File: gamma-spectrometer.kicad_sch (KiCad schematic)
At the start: 36 parts, among them T1 T1-1T-KK81, U1 Pico 2, U2 MAX1422ECM+D, U3 TLV3201AIDBVR, U4 MAX5026EUT_T

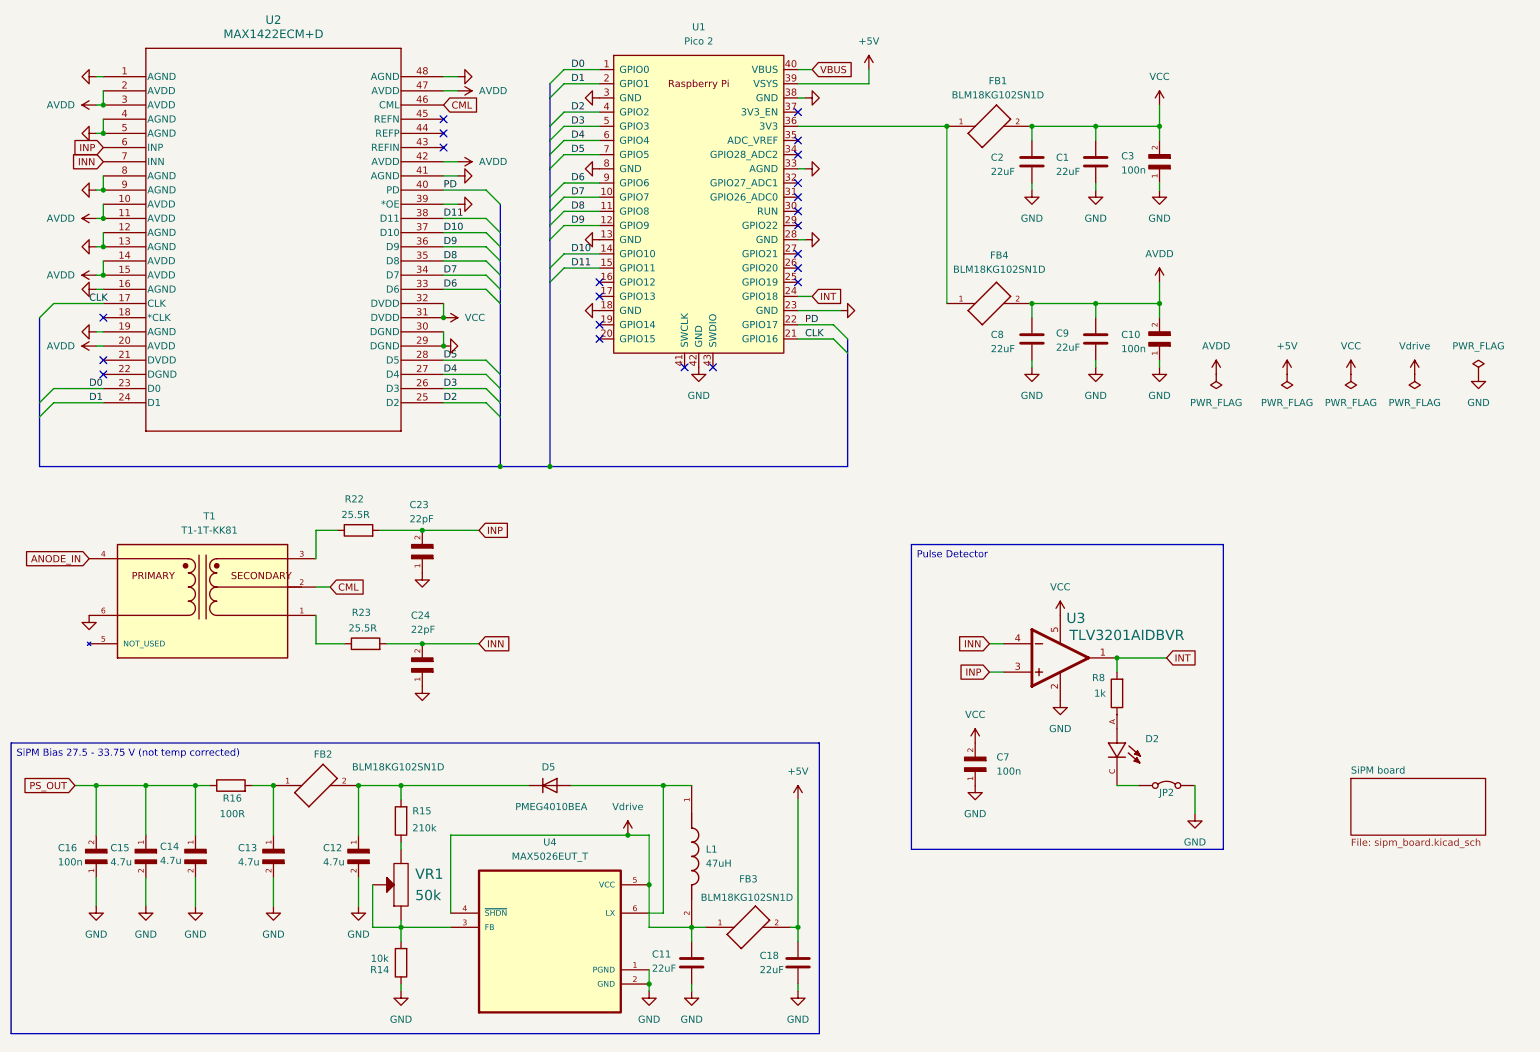
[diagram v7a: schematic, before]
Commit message: MCP41050 replaces pot for SiPM PS regulation
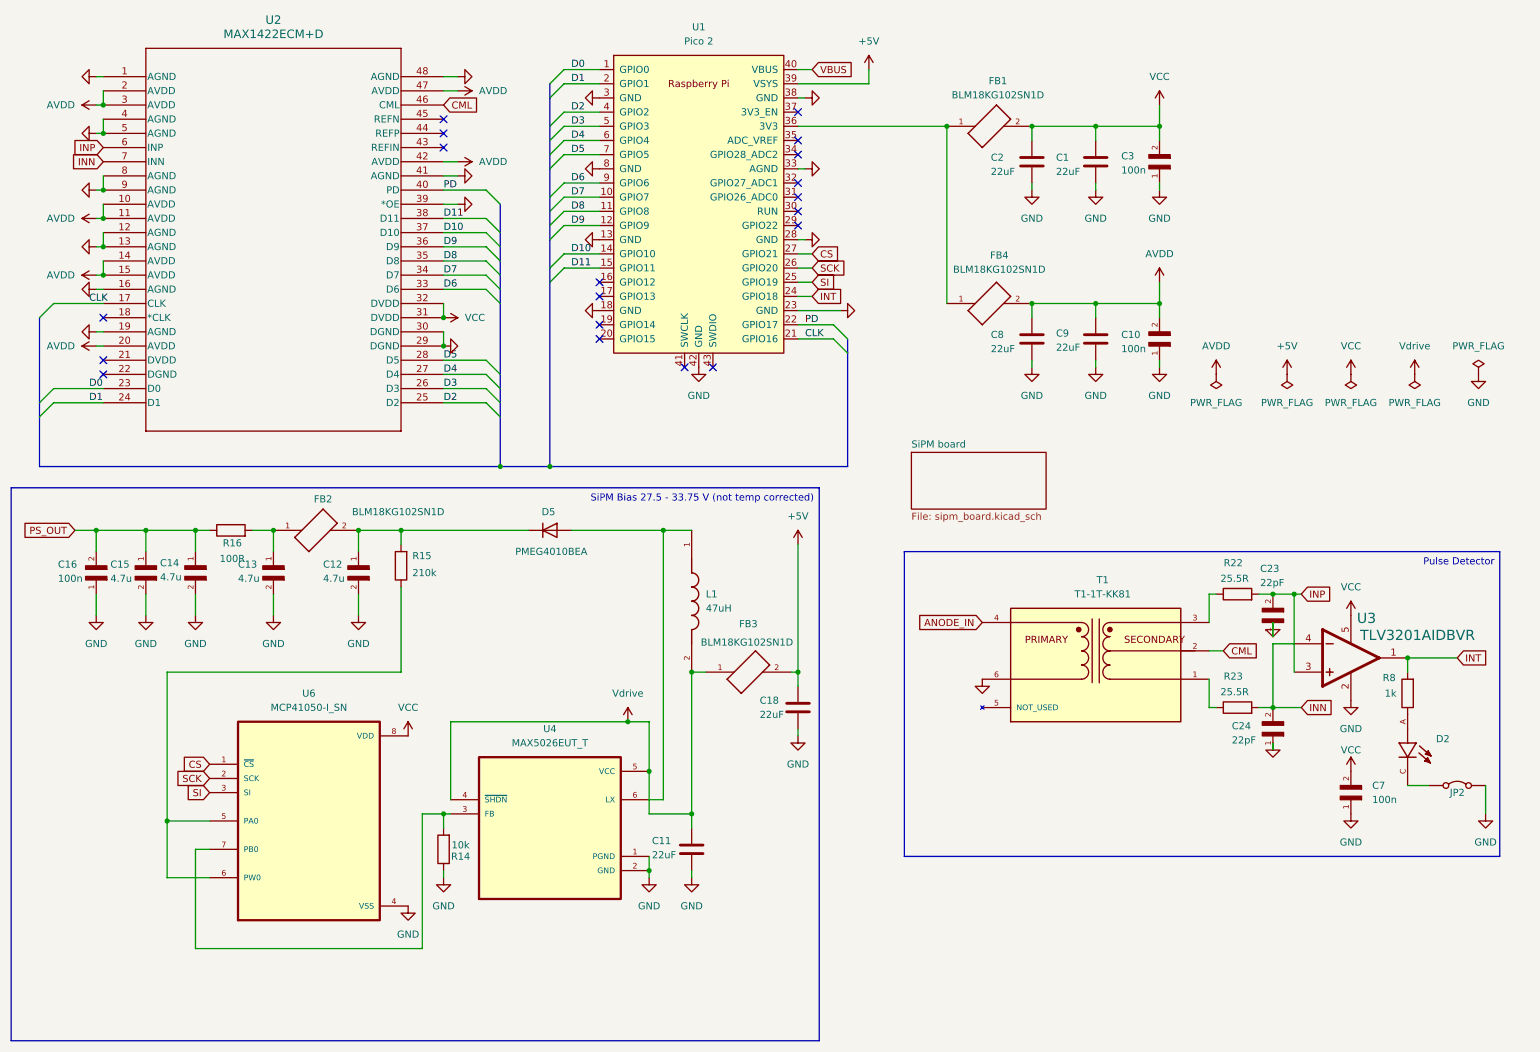
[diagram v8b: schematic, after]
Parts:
- removed VR1: 50k, 3266W-1-503:TRIM_3266W-1-503, symbol 3296W-1-503LF:3296W-1-503LF
- added U6: MCP41050-I_SN, MCP41050-I_SN:SOIC127P600X175-8N, symbol MCP41050-I_SN:MCP41050-I_SN
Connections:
- net GND: now also U6.4 (VSS)
- net VCC: now also U6.8 (VDD)
- net at R14.2, U4.3 (FB): now also U6.7 (PB0)
- net at R15.1: now also U6.5 (PA0), U6.6 (PW0)
- net SI: now reaches U1.25 (GPIO19)
- net SI: now also U6.3 (SI)
- net SCK: now reaches U1.26 (GPIO20)
- net SCK: now also U6.2 (SCK)
- net CS: now reaches U1.27 (GPIO21)
- net CS: now also U6.1 (~{CS})
- no-connect marks 22 -> 19
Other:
- moved on the sheet: C11, C12, C13, C14, C15, C16, C18, C23, C24, C7, D2, D5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
